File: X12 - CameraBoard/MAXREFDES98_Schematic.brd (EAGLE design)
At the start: 78.9 x 25.4 mm, 24 parts, among them U1 MB110S-TP, U2 MB110S-TP, U3 MAX5969AETB+, U4 MAX17503ATP+

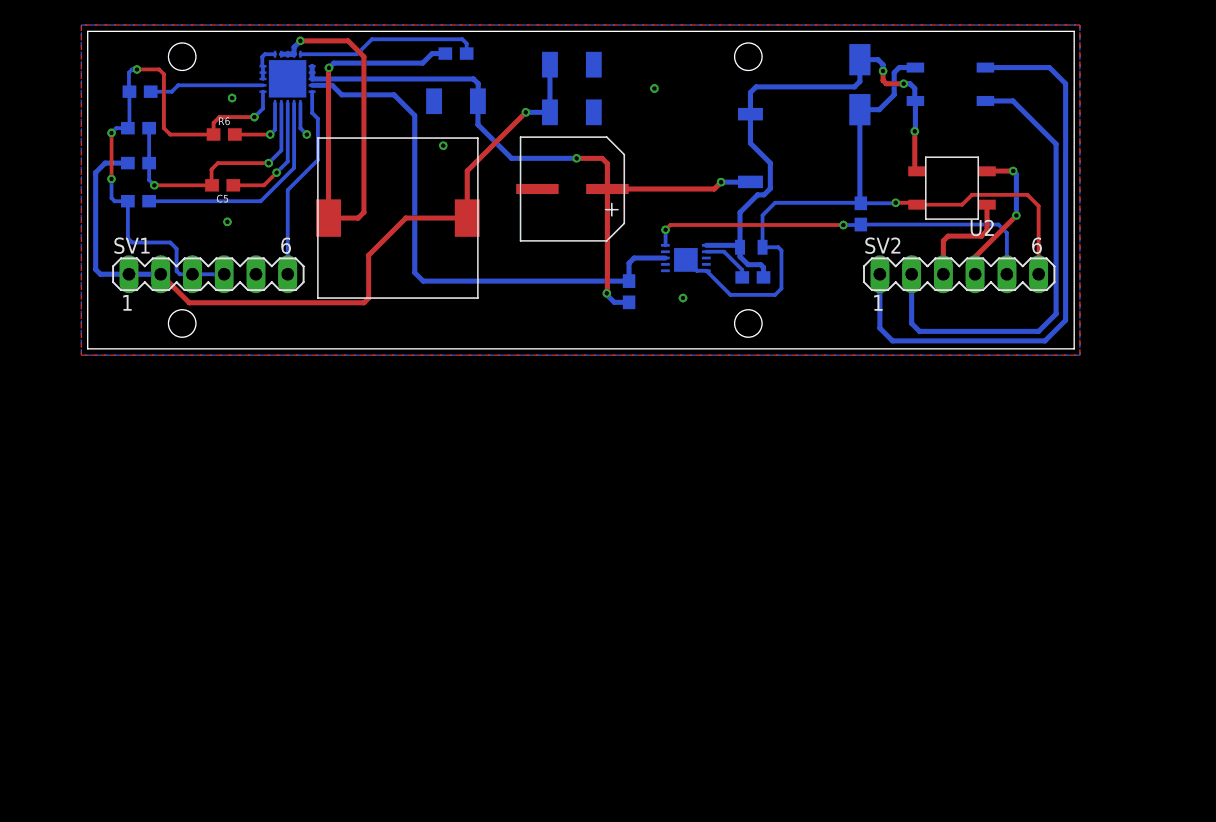
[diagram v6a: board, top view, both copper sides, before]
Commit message: Added New Connector and PI
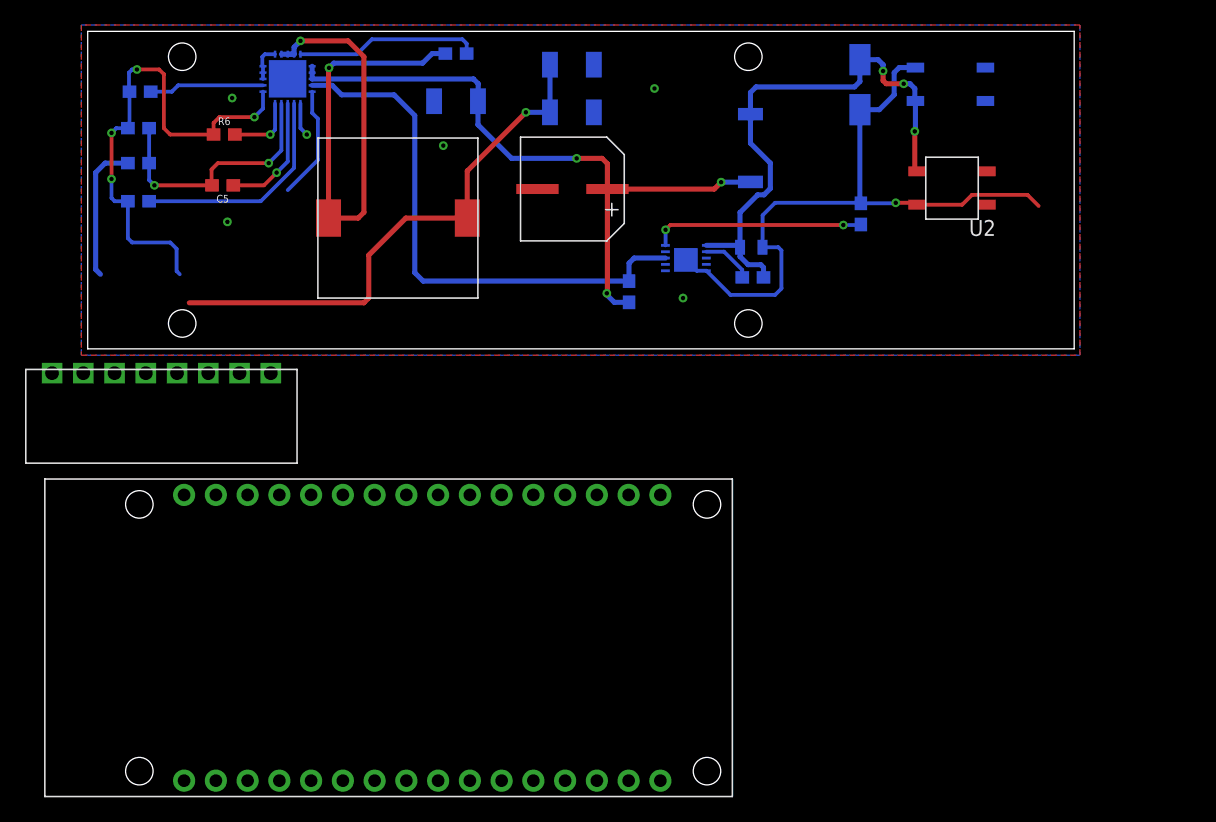
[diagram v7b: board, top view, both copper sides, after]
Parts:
- removed SV1, SV2: (no value), con-lstb:MA06-1
- added CONN: TERM_BLOCK_PLUG_8POS_STR_2.5MM, Camera_Board_Parts_09_30_2020:TERM_BLOCK_PLUG_8POS_STR_2.5MM
- added U$2: NANO_PI, Camera_Board_Parts_09_30_2020:NANO_PI
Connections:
- removed net CLS: R1.2, SV2.5, U3.10
- removed net RECT_A_INPUT_1: SV2.1, U1.~1
- removed net RECT_A_INPUT_2: SV2.2, U1.~2
- removed net RECT_B_INPUT_1: SV2.3, U2.~1
- removed net RECT_B_INPUT_2: SV2.4, U2.~2
- new net 5V_OUT5: CONN.5
- new net N$4: R1.2, U3.10
- new net N$8: U$2.3V3
- new net RECT1_IN_MINUS: CONN.1, U1.~1
- new net RECT1_IN_PLUS: CONN.2, U1.~2
- new net RECT2_IN_MINUS: CONN.3, U2.~1
- new net RECT2_IN_PLUS: CONN.4, U2.~2
- net 5V_OUT: now also CONN.6, U$2.5V, U$2.5V_2; no longer SV1.1, SV1.2
- net GND: now also CONN.7, CONN.8, U$2.GND; no longer SV1.3, SV1.4
- net RESET: no longer SV1.6
- net VSS_EP: no longer SV2.6
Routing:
- net RECT_A_INPUT_1: track 46.2 -> 0.00 mm
- net RECT_A_INPUT_2: track 37.0 -> 0.00 mm
- net CLS: track 32.3 -> 0.00 mm, vias 2 -> 0
- net N$4: track 0.00 -> 17.0 mm, vias 0 -> 2
- net RECT_B_INPUT_2: track 11.8 -> 0.00 mm, vias 2 -> 0
- net RECT_B_INPUT_1: track 8.57 -> 0.00 mm
- net 5V_OUT: track 62.4 -> 54.4 mm
- net RESET: track 15.8 -> 9.06 mm
- net VSS_EP: track 59.3 -> 53.9 mm
- net GND: track 49.4 -> 45.8 mm

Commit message: Added 0 Ohm Resistor amd 1-pin connector directly to 5V line
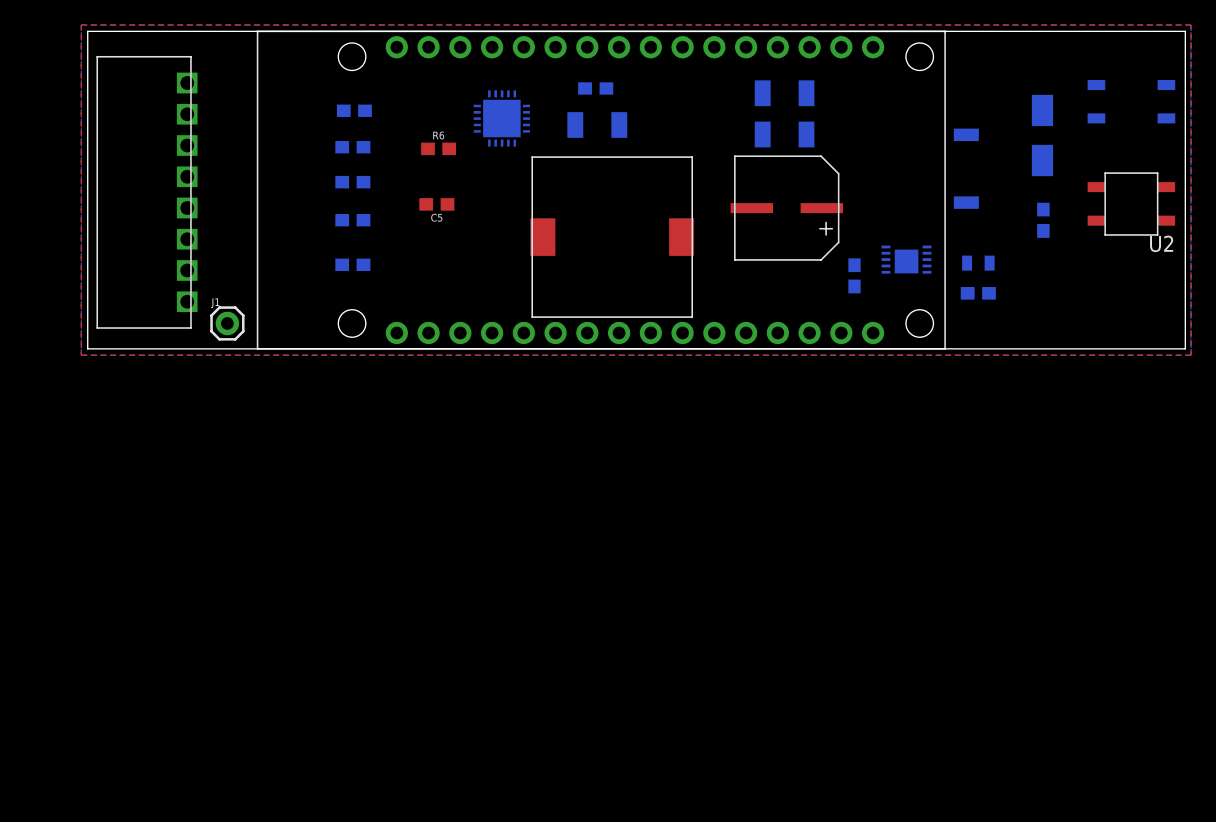
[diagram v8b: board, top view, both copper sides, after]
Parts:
- added J1: (no value), SparkFun-Connectors:1X01
- added R7: 0, SparkFun-Resistors:0603
- moved U$2 39.7 mm to (13.6, 0.00)
- moved CONN 33.0 mm to (0.76, 23.4), turned to 270 degrees
- moved C1 18.2 mm to (71.2, 6.86)
- moved R2 18.1 mm to (71.2, 4.45)
- moved R3 18.1 mm to (61.3, 5.84)
- moved U3 17.7 mm to (67.1, 5.59)
- moved U4 17.4 mm to (35.2, 16.4)
- moved L1 17.4 mm to (73.2, 17.3)
- moved C5 17.2 mm to (27.9, 11.6)
- moved L2 17.2 mm to (35.6, 2.54)
- moved C6 17.2 mm to (21.2, 10.3)
- moved C8 17.2 mm to (21.3, 19.1)
- moved R4 17.2 mm to (21.2, 13.3)
- moved R5 17.2 mm to (21.2, 16.1)
- moved C2 17.2 mm to (60.1, 7.11)
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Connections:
- net 5V_OUT5 renamed RXD
- new net IND_2_OUT: C10.1, C4.1, L2.P$2, R4.2, R7.1
- new net TXD: CONN.6
- net 5V_OUT: now also J1.1, R7.2; no longer C10.1, C4.1, CONN.6, L2.P$2, R4.2
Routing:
- net 5V_OUT: track 54.4 -> 0.00 mm, vias 1 -> 0
- net VSS_EP: track 53.9 -> 0.00 mm, vias 1 -> 0
- net VIN: track 53.6 -> 0.00 mm, vias 3 -> 0
- net GND: track 45.8 -> 0.00 mm, vias 10 -> 0
- net LX: track 45.7 -> 0.00 mm, vias 2 -> 0
- net VDD: track 44.7 -> 0.00 mm, vias 3 -> 0
- net PG_EN/UVLO: track 43.7 -> 0.00 mm
- net FB: track 20.6 -> 0.00 mm, vias 2 -> 0
- net SS: track 17.9 -> 0.00 mm
- net N$4: track 17.0 -> 0.00 mm, vias 2 -> 0
- net BST: track 14.7 -> 0.00 mm
- net CF: track 9.79 -> 0.00 mm, vias 1 -> 0
- net VCC: track 9.19 -> 0.00 mm
- net RESET: track 9.06 -> 0.00 mm
- net RT: track 5.48 -> 0.00 mm, vias 1 -> 0
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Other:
- board size 78.9 x 25.4 mm -> 87.8 x 25.4 mm
